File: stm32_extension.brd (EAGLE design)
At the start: 2 parts

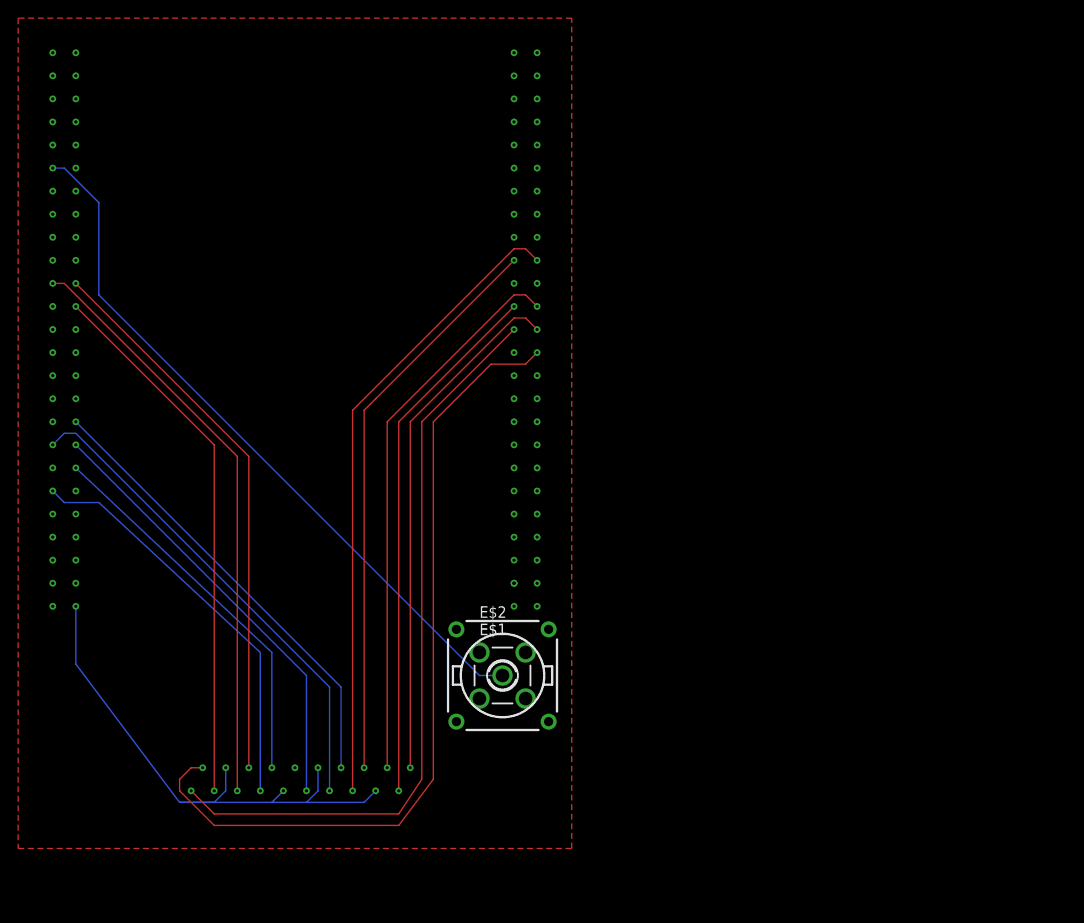
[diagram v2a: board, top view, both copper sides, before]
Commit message: Added 2 GND planes. Input using VIAs. :
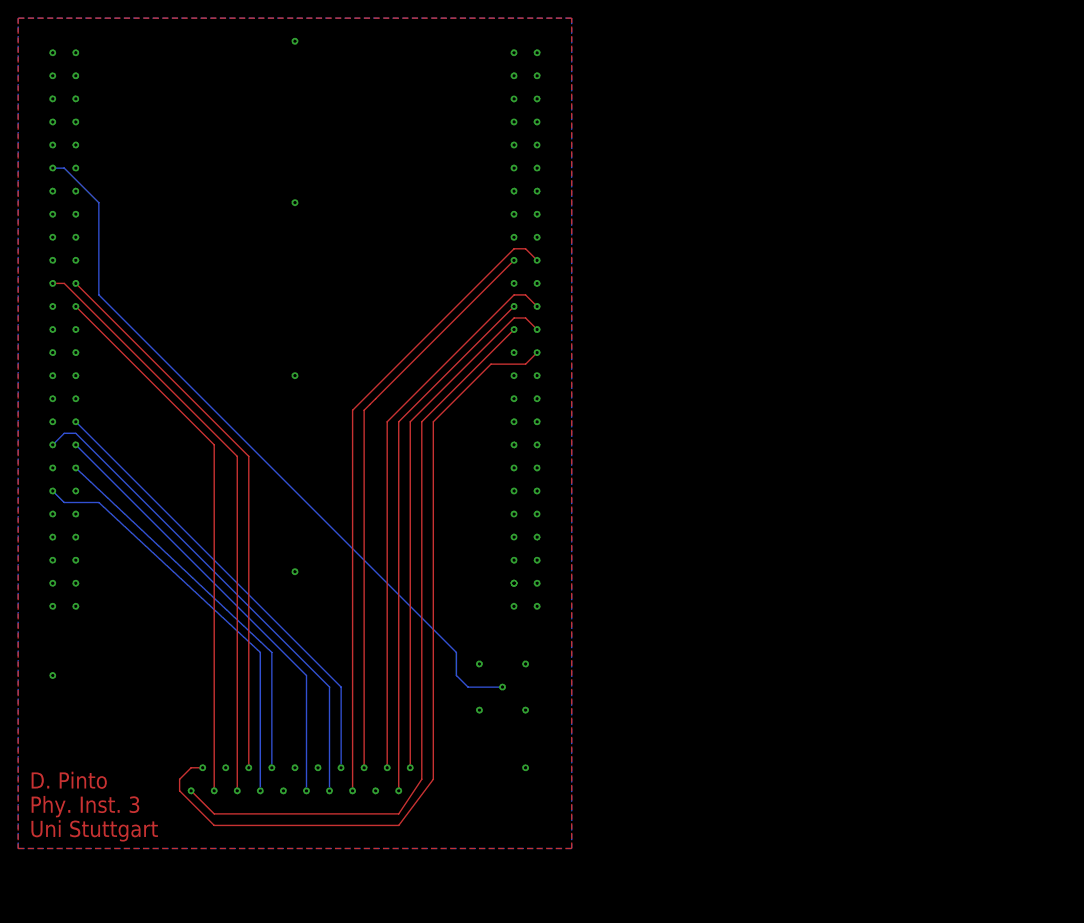
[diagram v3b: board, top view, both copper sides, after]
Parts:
- removed E$1: (no value), con-coax:LTI-SASF54GT
- removed E$2: (no value), con-coax:A1944
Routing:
- net S$9: track 25.7 -> 0.00 mm
- net S$72: track 25.4 -> 0.00 mm
- net S$139: track 8.15 -> 0.00 mm, vias 1 -> 0
- net S$15: track 0.00 -> 5.61 mm, vias 0 -> 1
- net S$59: track 78.6 -> 75.0 mm
- net S$4: track 2.54 -> 0.00 mm, vias 1 -> 0
- added copper zone on layer 16, net GND
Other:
- board text added: "D. Pinto Phy. Inst. 3 Uni Stuttgart"
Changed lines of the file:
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@@
 <layer number="41" name="tRestrict" color="4" fill="10" visible="yes" active="yes"/>
 <layer number="42" name="bRestrict" color="1" fill="10" visible="yes" active="yes"/>
-<layer number="43" name="vRestrict" color="2" fill="10" visible="yes" active="yes"/>
-<layer number="44" name="Drills" color="7" fill="1" visible="no" active="yes"/>
+<layer number="43" name="vRestrict" color="2" fill="10" visible="no" active="yes"/>
+<layer number="44" name="Drills" color="7" fill="1" visible="yes" active="yes"/>
 <layer number="45" name="Holes" color="7" fill="1" visible="yes" active="yes"/>
 <layer number="46" name="Milling" color="3" fill="1" visible="no" active="yes"/>
 <layer number="47" name="Measures" color="7" fill="1" visible="no" active="yes"/>
-<layer number="48" name="Document" color="7" fill="1" visible="yes" active="yes"/>
-<layer number="49" name="Reference" color="7" fill="1" visible="yes" active="yes"/>
+<layer number="48" name="Document" color="7" fill="1" visible="no" active="yes"/>
+<layer number="49" name="Reference" color="7" fill="1" visible="no" active="yes"/>
 <layer number="51" name="tDocu" color="7" fill="1" visible="yes" active="yes"/>
 <layer number="52" name="bDocu" color="7" fill="1" visible="yes" active="yes"/>
@@
 <board>
 <plain>
+<text x="-27.94" y="-12.7" size="1.778" layer="1">D. Pinto
+Phy. Inst. 3
+Uni Stuttgart</text>
+<dimension x1="-33.02" y1="77.47" x2="-33.02" y2="-13.97" x3="-33.02" y3="31.75" textsize="1.778" layer="1"/>
+<dimension x1="-29.21" y1="80.01" x2="31.75" y2="80.01" x3="1.27" y3="80.01" textsize="1.778" layer="1"/>
 </plain>
 <attributes>
@@
 </class>
 </classes>
-<designrules name="default">
+<designrules name="default *">
 <description language="de">&lt;b&gt;EAGLE Design Rules&lt;/b&gt;
 &lt;p&gt;
@@
 <param name="rvMicroViaOuter" value="0.25"/>
 <param name="rvMicroViaInner" value="0.25"/>
-<param name="rlMinPadTop" value="10mil"/>
+<param name="rlMinPadTop" value="12mil"/>
 <param name="rlMaxPadTop" value="20mil"/>
 <param name="rlMinPadInner" value="10mil"/>
 <param name="rlMaxPadInner" value="20mil"/>
-<param name="rlMinPadBottom" value="10mil"/>
+<param name="rlMinPadBottom" value="12mil"/>
 <param name="rlMaxPadBottom" value="20mil"/>
 <param name="rlMinViaOuter" value="8mil"/>
@@
 </autorouter>
 <elements>
-<element name="E$1" library="con-coax" library_urn="urn:adsk.eagle:library:133" package="LTI-SASF54GT" value="" x="24.13" y="5.08"/>
-<element name="E$2" library="con-coax" library_urn="urn:adsk.eagle:library:133" package="A1944" value="" x="24.13" y="5.08"/>
 </elements>
 <signals>
-<signal name="S$21">
-<via x="-25.4" y="12.7" extent="1-16" drill="0.35"/>
-</signal>
-<signal name="S$22">
-<via x="-22.86" y="12.7" extent="1-16" drill="0.35"/>
-</signal>
 <signal name="S$23">
 <via x="-25.4" y="15.24" extent="1-16" drill="0.35"/>
@@
 <via x="-25.4" y="33.02" extent="1-16" drill="0.35"/>
 </signal>
-<signal name="S$39">
-<via x="-25.4" y="35.56" extent="1-16" drill="0.35"/>
-</signal>
 <signal name="S$40">
 <via x="-22.86" y="35.56" extent="1-16" drill="0.35"/>
 </signal>
-<signal name="S$41">
-<via x="-25.4" y="38.1" extent="1-16" drill="0.35"/>
-</signal>
 <signal name="S$42">
 <via x="-22.86" y="38.1" extent="1-16" drill="0.35"/>
@@
 <signal name="S$46">
 <via x="-22.86" y="43.18" extent="1-16" drill="0.35"/>
-</signal>
-<signal name="S$47">
-<via x="-25.4" y="45.72" extent="1-16" drill="0.35"/>
 </signal>
 <signal name="S$48">
@@
 <wire x1="-24.13" y1="60.96" x2="-20.32" y2="57.15" width="0.1524" layer="16"/>
 <wire x1="-20.32" y1="57.15" x2="-20.32" y2="46.99" width="0.1524" layer="16"/>
-<wire x1="-20.32" y1="46.99" x2="21.59" y2="5.08" width="0.1524" layer="16"/>
-<wire x1="21.59" y1="5.08" x2="24.13" y2="5.08" width="0.1524" layer="16"/>
+<wire x1="-20.32" y1="46.99" x2="19.05" y2="7.62" width="0.1524" layer="16"/>
+<wire x1="19.05" y1="7.62" x2="19.05" y2="5.08" width="0.1524" layer="16"/>
 </signal>
 <signal name="S$60">
@@
 <via x="-22.86" y="66.04" extent="1-16" drill="0.35"/>
 </signal>
-<signal name="S$65">
-<via x="-25.4" y="68.58" extent="1-16" drill="0.35"/>
-</signal>
 <signal name="S$66">
 <via x="-22.86" y="68.58" extent="1-16" drill="0.35"/>
@@
 <via x="-22.86" y="71.12" extent="1-16" drill="0.35"/>
 </signal>
-<signal name="S$69">
-<via x="-25.4" y="73.66" extent="1-16" drill="0.35"/>
-</signal>
-<signal name="S$70">
-<via x="-22.86" y="73.66" extent="1-16" drill="0.35"/>
-</signal>
 <signal name="S$2">
 <via x="25.4" y="15.24" extent="1-16" drill="0.35"/>
 </signal>
-<signal name="S$6">
-<via x="27.94" y="12.7" extent="1-16" drill="0.35"/>
-</signal>
-<signal name="S$9">
-<wire x1="-6.35" y1="-5.08" x2="-6.35" y2="-7.62" width="0.1524" layer="16"/>
-<wire x1="-6.35" y1="-7.62" x2="-7.62" y2="-8.89" width="0.1524" layer="16"/>
-<wire x1="-7.62" y1="-8.89" x2="-11.43" y2="-8.89" width="0.1524" layer="16"/>
-<wire x1="-11.43" y1="-8.89" x2="-1.27" y2="-8.89" width="0.1524" layer="16"/>
-<wire x1="-1.27" y1="-8.89" x2="0" y2="-7.62" width="0.1524" layer="16"/>
-<wire x1="-1.27" y1="-8.89" x2="2.54" y2="-8.89" width="0.1524" layer="16"/>
-<wire x1="2.54" y1="-8.89" x2="3.81" y2="-7.62" width="0.1524" layer="16"/>
-</signal>
-<signal name="S$72">
-<wire x1="-11.43" y1="-8.89" x2="-22.86" y2="6.35" width="0.1524" layer="16"/>
-<wire x1="-22.86" y1="6.35" x2="-22.86" y2="12.7" width="0.1524" layer="16"/>
-</signal>
 <signal name="S$73">
 <via x="25.4" y="15.24" extent="1-16" drill="0.35"/>
@@
 <signal name="S$118">
 <via x="27.94" y="71.12" extent="1-16" drill="0.35"/>
-</signal>
-<signal name="S$119">
-<via x="25.4" y="73.66" extent="1-16" drill="0.35"/>
-</signal>
-<signal name="S$120">
-<via x="27.94" y="73.66" extent="1-16" drill="0.35"/>
-</signal>
-<signal name="S$121">
-<via x="-6.35" y="-5.08" extent="1-16" drill="0.35"/>
 </signal>
 <signal name="S$122">
@@
 <signal name="S$124">
 <via x="1.27" y="-5.08" extent="1-16" drill="0.35"/>
-</signal>
-<signal name="S$4">
-<via x="3.81" y="-5.08" extent="1-16" drill="0.35"/>
-<wire x1="3.81" y1="-5.08" x2="3.81" y2="-7.62" width="0.1524" layer="16"/>
 </signal>
 <signal name="S$126">
@@
 <via x="-2.54" y="-7.62" extent="1-16" drill="0.35"/>
 </signal>
-<signal name="S$135">
-<via x="0" y="-7.62" extent="1-16" drill="0.35"/>
-</signal>
 <signal name="S$136">
 <via x="2.54" y="-7.62" extent="1-16" drill="0.35"/>
@@
 <wire x1="26.67" y1="52.07" x2="27.94" y2="50.8" width="0.1524" layer="1"/>
 </signal>
-<signal name="S$139">
-<via x="10.16" y="-7.62" extent="1-16" drill="0.35"/>
-<wire x1="10.16" y1="-7.62" x2="8.89" y2="-8.89" width="0.1524" layer="16"/>
-<wire x1="8.89" y1="-8.89" x2="2.54" y2="-8.89" width="0.1524" layer="16"/>
-</signal>
 <signal name="S$140">
 <via x="12.7" y="-7.62" extent="1-16" drill="0.35"/>
@@
 <wire x1="12.7" y1="33.02" x2="25.4" y2="45.72" width="0.1524" layer="1"/>
 </signal>
-<signal name="S$1">
-<via x="25.4" y="12.7" extent="1-16" drill="0.35"/>
-</signal>
 <signal name="GND">
-<polygon width="0.2" layer="1" isolate="0.3048">
+<polygon width="0.1524" layer="1" isolate="0.3048">
 <vertex x="31.75" y="-13.97"/>
 <vertex x="31.75" y="77.47"/>
@@
 <vertex x="-29.21" y="-13.97"/>
 </polygon>
+<via x="1.27" y="16.51" extent="1-16" drill="0.35"/>
+<via x="-25.4" y="5.08" extent="1-16" drill="0.35"/>
+<via x="26.67" y="-5.08" extent="1-16" drill="0.35"/>
+<polygon width="0.1524" layer="16" isolate="0.3048">
+<vertex x="-29.21" y="77.47"/>
+<vertex x="31.75" y="77.47"/>
+<vertex x="31.75" y="-13.97"/>
+<vertex x="-29.21" y="-13.97"/>
+</polygon>
+<via x="-22.86" y="12.7" extent="1-16" drill="0.35"/>
+<via x="25.4" y="12.7" extent="1-16" drill="0.35"/>
+<via x="0" y="-7.62" extent="1-16" drill="0.35"/>
+<via x="26.67" y="6.35" extent="1-16" drill="0.35"/>
+<via x="26.67" y="1.27" extent="1-16" drill="0.35"/>
+<via x="21.59" y="1.27" extent="1-16" drill="0.35"/>
+<via x="21.59" y="6.35" extent="1-16" drill="0.35"/>
+<via x="-6.35" y="-5.08" extent="1-16" drill="0.35"/>
+<via x="3.81" y="-5.08" extent="1-16" drill="0.35"/>
+<via x="10.16" y="-7.62" extent="1-16" drill="0.35"/>
+<via x="-22.86" y="73.66" extent="1-16" drill="0.35"/>
+<via x="-25.4" y="73.66" extent="1-16" drill="0.35"/>
+<via x="25.4" y="73.66" extent="1-16" drill="0.35"/>
+<via x="27.94" y="73.66" extent="1-16" drill="0.35"/>
+<via x="27.94" y="12.7" extent="1-16" drill="0.35"/>
+<via x="-25.4" y="12.7" extent="1-16" drill="0.35"/>
+<via x="-25.4" y="45.72" extent="1-16" drill="0.35"/>
+<via x="-25.4" y="68.58" extent="1-16" drill="0.35"/>
+</signal>
+<signal name="S$11">
+<via x="-25.4" y="38.1" extent="1-16" drill="0.35"/>
+</signal>
+<signal name="S$12">
+<via x="-25.4" y="35.56" extent="1-16" drill="0.35"/>
+</signal>
+<signal name="S$13">
+<via x="1.27" y="74.93" extent="1-16" drill="0.35"/>
+</signal>
+<signal name="S$14">
+<via x="1.27" y="57.15" extent="1-16" drill="0.35"/>
+</signal>
+<signal name="S$17">
+<via x="1.27" y="38.1" extent="1-16" drill="0.35"/>
+</signal>
+<signal name="S$15">
+<via x="24.13" y="3.81" extent="1-16" drill="0.35"/>
+<wire x1="24.13" y1="3.81" x2="20.32" y2="3.81" width="0.1524" layer="16"/>
+<wire x1="20.32" y1="3.81" x2="19.05" y2="5.08" width="0.1524" layer="16"/>
 </signal>
 </signals>
@@
 </drawing>
 <compatibility>
-<note version="8.2" severity="warning">
-Since Version 8.2, Eagle supports online libraries. The ids
-of those online libraries will not be understood (or retained)
-with this version.
+<note version="6.3" minversion="6.2.2" severity="warning">
+Since Version 6.2.2 text objects can contain more than one line,
+which will not be processed correctly with this version.
 </note>
 </compatibility>
